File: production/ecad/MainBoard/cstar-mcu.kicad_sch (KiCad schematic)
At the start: 61 parts, among them J1 USB_C_Receptacle_USB2.0, J25 TYPE-C-31-M-12, J3 RX connect, J31 TYPE-C-31-M-12, J4 TX connect, J5 Ultra_1, J6 Ultra_2, J7 Ultra_3, J8 Ultra_4, Q1 AO3400A, Q2 AO3400A, Q3 AO3400A, Q4 AO3400A, SW1 SW_Push, SW2 SW_Push, SW3 SW_Push, SW4 SW_Push, U1 ESP32-WROOM-32UE_M113EH6400UH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, U2 CP2102N-A01-GQFN28, U3 TXB0104DR, U4 CP2102N-A01-GQFN28, U5 TXB0104DR, U6 ESP32-WROOM-32UE_M113EH6400UH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

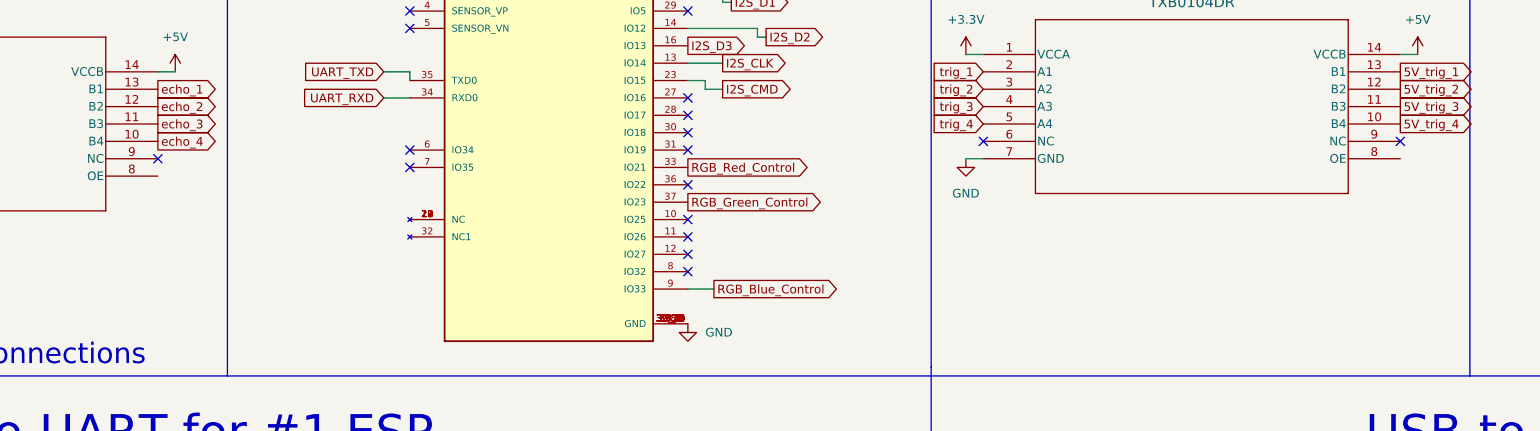
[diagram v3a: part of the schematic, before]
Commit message: OE to ground
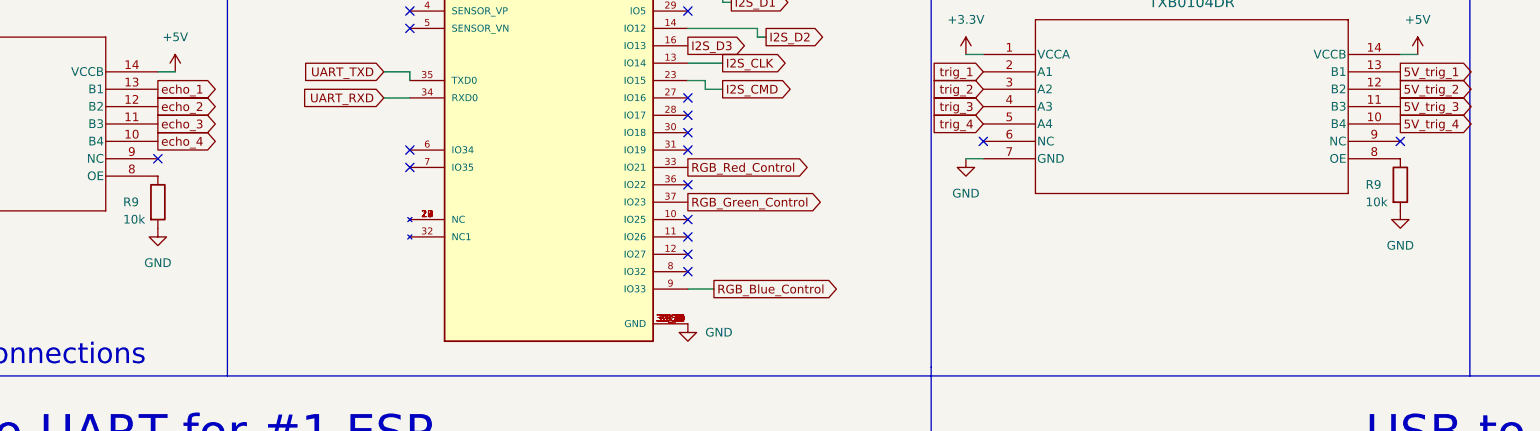
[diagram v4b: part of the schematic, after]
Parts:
- added R9 (x2): 10k, Resistor_SMD:R_0805_2012Metric, symbol Device:R
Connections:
- net GND: now also R9.2, R9.2
- net at U5.8 (OE): now also R9.1
- net at U3.8 (OE): now also R9.1
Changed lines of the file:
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@@
+    )
+  )
+  (symbol (lib_id "Device:R") (at 96.52 71.12 0) (unit 1)
+    (in_bom yes) (on_board yes) (dnp no)
+    (property "Reference" "R9" (at 91.44 71.12 0)
+      (effects (font (size 1.27 1.27)) (justify left))
+    )
+    (property "Value" "10k" (at 91.44 73.66 0)
+      (effects (font (size 1.27 1.27)) (justify left))
+    )
+    (property "Footprint" "Resistor_SMD:R_0805_2012Metric" (at 94.742 71.12 90)
+      (effects (font (size 1.27 1.27)) hide)
+    )
+    (property "Datasheet" "~" (at 96.52 71.12 0)
+      (effects (font (size 1.27 1.27)) hide)
+    )
+    (pin "1")
+    (pin "2")
+    (instances
+      (project "cstar-mcu"
+        (path "/889d461f-2713-421f-88e2-0d0ce2e66089"
+          (reference "R9") (unit 1)
+        )
+      )
+      (project "CSTAR"
+        (path "/cd9fa943-c6eb-468b-990c-ea873c442553/ab376fb8-b3cc-4961-835f-6ea621157706"
+          (reference "R45") (unit 1)
+        )
+      )
     )
   )
@@
         (path "/cd9fa943-c6eb-468b-990c-ea873c442553/ab376fb8-b3cc-4961-835f-6ea621157706"
           (reference "R49") (unit 1)
+        )
+      )
+    )
+  )
+  (symbol (lib_id "power:GND") (at 96.52 74.93 0) (unit 1)
+    (in_bom yes) (on_board yes) (dnp no) (fields_autoplaced)
+    (property "Reference" "#PWR038" (at 96.52 81.28 0)
+      (effects (font (size 1.27 1.27)) hide)
+    )
+    (property "Value" "GND" (at 96.52 80.01 0)
+      (effects (font (size 1.27 1.27)))
+    )
+    (property "Footprint" "" (at 96.52 74.93 0)
+      (effects (font (size 1.27 1.27)) hide)
+    )
+    (property "Datasheet" "" (at 96.52 74.93 0)
+      (effects (font (size 1.27 1.27)) hide)
+    )
+    (pin "1")
+    (instances
+      (project "cstar-mcu"
+        (path "/889d461f-2713-421f-88e2-0d0ce2e66089"
+          (reference "#PWR038") (unit 1)
+        )
+      )
+      (project "CSTAR"
+        (path "/cd9fa943-c6eb-468b-990c-ea873c442553/ab376fb8-b3cc-4961-835f-6ea621157706"
+          (reference "#PWR0110") (unit 1)
         )
       )
@@
     )
   )
+  (symbol (lib_id "Device:R") (at 278.13 68.58 0) (unit 1)
+    (in_bom yes) (on_board yes) (dnp no)
+    (property "Reference" "R9" (at 273.05 68.58 0)
+      (effects (font (size 1.27 1.27)) (justify left))
+    )
+    (property "Value" "10k" (at 273.05 71.12 0)
+      (effects (font (size 1.27 1.27)) (justify left))
+    )
+    (property "Footprint" "Resistor_SMD:R_0805_2012Metric" (at 276.352 68.58 90)
+      (effects (font (size 1.27 1.27)) hide)
+    )
+    (property "Datasheet" "~" (at 278.13 68.58 0)
+      (effects (font (size 1.27 1.27)) hide)
+    )
+    (pin "1")
+    (pin "2")
+    (instances
+      (project "cstar-mcu"
+        (path "/889d461f-2713-421f-88e2-0d0ce2e66089"
+          (reference "R9") (unit 1)
+        )
+      )
+      (project "CSTAR"
+        (path "/cd9fa943-c6eb-468b-990c-ea873c442553/ab376fb8-b3cc-4961-835f-6ea621157706"
+          (reference "R43") (unit 1)
+        )
+      )
+    )
+  )
   (symbol (lib_id "power:+5V") (at 24.13 15.24 90) (unit 1)
     (in_bom yes) (on_board yes) (dnp no) (fields_autoplaced)
@@
         )
       )
+    )
+  )
+  (symbol (lib_id "power:GND") (at 278.13 72.39 0) (unit 1)
+    (in_bom yes) (on_board yes) (dnp no) (fields_autoplaced)
+    (property "Reference" "#PWR038" (at 278.13 78.74 0)
+      (effects (font (size 1.27 1.27)) hide)
+    )
+    (property "Value" "GND" (at 278.13 77.47 0)
+      (effects (font (size 1.27 1.27)))
+    )
+    (property "Footprint" "" (at 278.13 72.39 0)
+      (effects (font (size 1.27 1.27)) hide)
+    )
+    (property "Datasheet" "" (at 278.13 72.39 0)
+      (effects (font (size 1.27 1.27)) hide)
+    )
+    (pin "1")
+    (instances
+      (project "cstar-mcu"
+        (path "/889d461f-2713-421f-88e2-0d0ce2e66089"
+          (reference "#PWR038") (unit 1)
+        )
+      )
+      (project "CSTAR"
+        (path "/cd9fa943-c6eb-468b-990c-ea873c442553/ab376fb8-b3cc-4961-835f-6ea621157706"
+          (reference "#PWR0113") (unit 1)
+        )
+      )

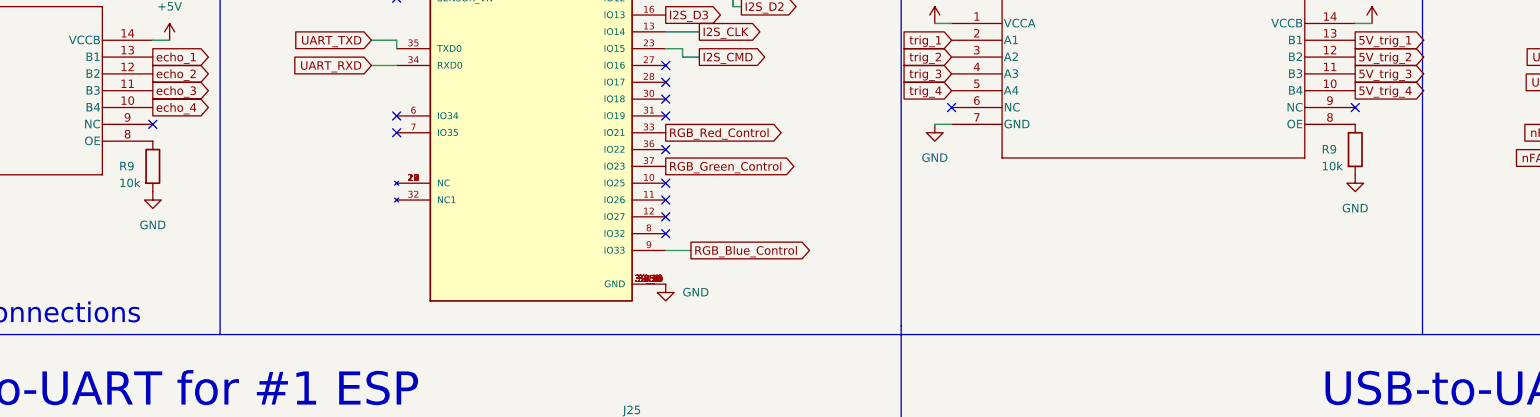
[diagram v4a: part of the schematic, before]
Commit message: fixed OE
talked to sean about the IC level shifter and fixed the open enable pin
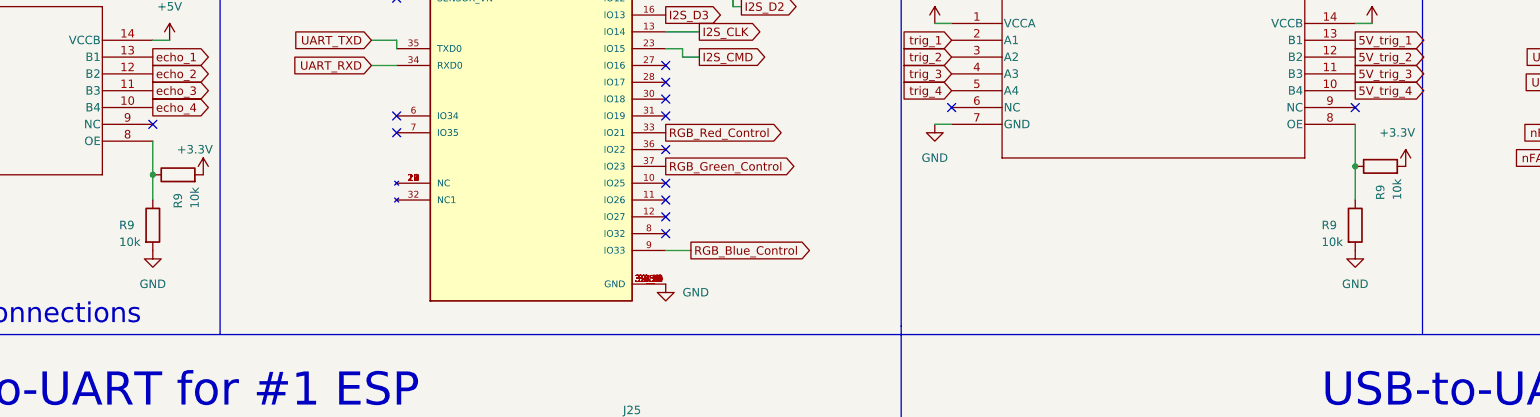
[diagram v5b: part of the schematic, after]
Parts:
- added R9 (x2): 10k, Resistor_SMD:R_0805_2012Metric, symbol Device:R
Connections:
- net +3.3V: now also R9.2, R9.2
- net at R9.1, U5.8 (OE): now also R9.1
- net at R9.1, U3.8 (OE): now also R9.1
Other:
- moved on the sheet: R9
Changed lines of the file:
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@@
   (junction (at 322.58 224.79) (diameter 0) (color 0 0 0 0)
   )
+  (junction (at 96.52 72.39) (diameter 0) (color 0 0 0 0)
+  )
   (junction (at 36.83 148.59) (diameter 0) (color 0 0 0 0)
   )
@@
   (junction (at 106.68 267.97) (diameter 0) (color 0 0 0 0)
   )
+  (junction (at 278.13 71.12) (diameter 0) (color 0 0 0 0)
+  )
   (junction (at 31.75 265.43) (diameter 0) (color 0 0 0 0)
   )
@@
     (stroke (width 0) (type default))
   )
+  (wire (pts (xy 278.13 71.12) (xy 278.13 64.77))
+    (stroke (width 0) (type default))
+  )
   (wire (pts (xy 361.95 33.02) (xy 370.84 33.02))
     (stroke (width 0) (type default))
@@
     (stroke (width 0) (type default))
   )
+  (wire (pts (xy 278.13 76.2) (xy 278.13 71.12))
+    (stroke (width 0) (type default))
+  )
   (wire (pts (xy 45.72 162.56) (xy 45.72 165.1))
     (stroke (width 0) (type default))
@@
     (stroke (width 0) (type default))
   )
+  (wire (pts (xy 96.52 72.39) (xy 96.52 67.31))
+    (stroke (width 0) (type default))
+  )
   (wire (pts (xy 173.99 148.59) (xy 181.61 148.59))
     (stroke (width 0) (type default))
@@
     (stroke (width 0) (type default))
   )
+  (wire (pts (xy 96.52 76.2) (xy 96.52 72.39))
+    (stroke (width 0) (type default))
+  )
   (wire (pts (xy 173.99 166.37) (xy 179.07 166.37))
     (stroke (width 0) (type default))
@@
     )
   )
+  (symbol (lib_id "Device:R") (at 100.33 72.39 90) (unit 1)
+    (in_bom yes) (on_board yes) (dnp no)
+    (property "Reference" "R9" (at 100.33 77.47 0)
+      (effects (font (size 1.27 1.27)) (justify left))
+    )
+    (property "Value" "10k" (at 102.87 77.47 0)
+      (effects (font (size 1.27 1.27)) (justify left))
+    )
+    (property "Footprint" "Resistor_SMD:R_0805_2012Metric" (at 100.33 74.168 90)
+      (effects (font (size 1.27 1.27)) hide)
+    )
+    (property "Datasheet" "~" (at 100.33 72.39 0)
+      (effects (font (size 1.27 1.27)) hide)
+    )
+    (pin "1")
+    (pin "2")
+    (instances
+      (project "cstar-mcu"
+        (path "/889d461f-2713-421f-88e2-0d0ce2e66089"
+          (reference "R9") (unit 1)
+        )
+      )
+      (project "CSTAR"
+        (path "/cd9fa943-c6eb-468b-990c-ea873c442553/ab376fb8-b3cc-4961-835f-6ea621157706"
+          (reference "R52") (unit 1)
+        )
+      )
+    )
+  )
   (symbol (lib_id "ESP32-WROOM-32UE_M113EH6400UH3Q0_:ESP32-WROOM-32UE_M113EH6400UH3Q0_") (at 341.63 63.5 0) (unit 1)
     (in_bom yes) (on_board yes) (dnp no) (fields_autoplaced)
@@
     )
   )
-  (symbol (lib_id "Device:R") (at 96.52 71.12 0) (unit 1)
+  (symbol (lib_id "Device:R") (at 96.52 80.01 0) (unit 1)
     (in_bom yes) (on_board yes) (dnp no)
-    (property "Reference" "R9" (at 91.44 71.12 0)
+    (property "Reference" "R9" (at 91.44 80.01 0)
       (effects (font (size 1.27 1.27)) (justify left))
     )
-    (property "Value" "10k" (at 91.44 73.66 0)
+    (property "Value" "10k" (at 91.44 82.55 0)
       (effects (font (size 1.27 1.27)) (justify left))
     )
-    (property "Footprint" "Resistor_SMD:R_0805_2012Metric" (at 94.742 71.12 90)
+    (property "Footprint" "Resistor_SMD:R_0805_2012Metric" (at 94.742 80.01 90)
       (effects (font (size 1.27 1.27)) hide)
     )
-    (property "Datasheet" "~" (at 96.52 71.12 0)
+    (property "Datasheet" "~" (at 96.52 80.01 0)
       (effects (font (size 1.27 1.27)) hide)
     )
@@
     )
   )
-  (symbol (lib_id "power:GND") (at 96.52 74.93 0) (unit 1)
+  (symbol (lib_id "power:GND") (at 96.52 83.82 0) (unit 1)
     (in_bom yes) (on_board yes) (dnp no) (fields_autoplaced)
-    (property "Reference" "#PWR038" (at 96.52 81.28 0)
+    (property "Reference" "#PWR038" (at 96.52 90.17 0)
       (effects (font (size 1.27 1.27)) hide)
     )
-    (property "Value" "GND" (at 96.52 80.01 0)
+    (property "Value" "GND" (at 96.52 88.9 0)
       (effects (font (size 1.27 1.27)))
     )
-    (property "Footprint" "" (at 96.52 74.93 0)
+    (property "Footprint" "" (at 96.52 83.82 0)
       (effects (font (size 1.27 1.27)) hide)
     )
-    (property "Datasheet" "" (at 96.52 74.93 0)
+    (property "Datasheet" "" (at 96.52 83.82 0)
       (effects (font (size 1.27 1.27)) hide)
     )
@@
     )
   )
+  (symbol (lib_id "power:+3.3V") (at 104.14 72.39 0) (unit 1)
+    (in_bom yes) (on_board yes) (dnp no)
+    (property "Reference" "#PWR0116" (at 104.14 76.2 0)
+      (effects (font (size 1.27 1.27)) hide)
+    )
+    (property "Value" "+3.3V" (at 102.87 68.58 0)
+      (effects (font (size 1.27 1.27)))
+    )
+    (property "Footprint" "" (at 104.14 72.39 0)
+      (effects (font (size 1.27 1.27)) hide)
+    )
+    (property "Datasheet" "" (at 104.14 72.39 0)
+      (effects (font (size 1.27 1.27)) hide)
+    )
+    (pin "1")
+    (instances
+      (project "CSTAR"
+        (path "/cd9fa943-c6eb-468b-990c-ea873c442553/ab376fb8-b3cc-4961-835f-6ea621157706"
+          (reference "#PWR0116") (unit 1)
+        )
+      )
+    )
+  )
   (symbol (lib_id "power:GND") (at 392.43 240.03 0) (unit 1)
     (in_bom yes) (on_board yes) (dnp no) (fields_autoplaced)
@@
     )
   )
-  (symbol (lib_id "Device:R") (at 278.13 68.58 0) (unit 1)
+  (symbol (lib_id "Device:R") (at 278.13 80.01 0) (unit 1)
     (in_bom yes) (on_board yes) (dnp no)
-    (property "Reference" "R9" (at 273.05 68.58 0)
+    (property "Reference" "R9" (at 273.05 80.01 0)
       (effects (font (size 1.27 1.27)) (justify left))
     )
-    (property "Value" "10k" (at 273.05 71.12 0)
+    (property "Value" "10k" (at 273.05 82.55 0)
       (effects (font (size 1.27 1.27)) (justify left))
     )
-    (property "Footprint" "Resistor_SMD:R_0805_2012Metric" (at 276.352 68.58 90)
+    (property "Footprint" "Resistor_SMD:R_0805_2012Metric" (at 276.352 80.01 90)
       (effects (font (size 1.27 1.27)) hide)
     )
-    (property "Datasheet" "~" (at 278.13 68.58 0)
+    (property "Datasheet" "~" (at 278.13 80.01 0)
       (effects (font (size 1.27 1.27)) hide)
     )
@@
     )
   )
+  (symbol (lib_id "power:+3.3V") (at 285.75 71.12 0) (unit 1)
+    (in_bom yes) (on_board yes) (dnp no)
+    (property "Reference" "#PWR0136" (at 285.75 74.93 0)
+      (effects (font (size 1.27 1.27)) hide)
+    )
+    (property "Value" "+3.3V" (at 284.48 66.04 0)
+      (effects (font (size 1.27 1.27)))
+    )
+    (property "Footprint" "" (at 285.75 71.12 0)
+      (effects (font (size 1.27 1.27)) hide)
+    )
+    (property "Datasheet" "" (at 285.75 71.12 0)
+      (effects (font (size 1.27 1.27)) hide)
+    )
+    (pin "1")
+    (instances
+      (project "CSTAR"
+        (path "/cd9fa943-c6eb-468b-990c-ea873c442553/ab376fb8-b3cc-4961-835f-6ea621157706"
+          (reference "#PWR0136") (unit 1)
+        )
+      )
+    )
+  )
   (symbol (lib_id "Device:R") (at 29.21 177.8 180) (unit 1)
     (in_bom yes) (on_board yes) (dnp no)
@@
     )
   )
+  (symbol (lib_id "Device:R") (at 281.94 71.12 90) (unit 1)
+    (in_bom yes) (on_board yes) (dnp no)
+    (property "Reference" "R9" (at 281.94 76.2 0)
+      (effects (font (size 1.27 1.27)) (justify left))
+    )
+    (property "Value" "10k" (at 284.48 76.2 0)
+      (effects (font (size 1.27 1.27)) (justify left))
+    )
+    (property "Footprint" "Resistor_SMD:R_0805_2012Metric" (at 281.94 72.898 90)
+      (effects (font (size 1.27 1.27)) hide)
+    )
+    (property "Datasheet" "~" (at 281.94 71.12 0)
+      (effects (font (size 1.27 1.27)) hide)
+    )
+    (pin "1")
+    (pin "2")
+    (instances
+      (project "cstar-mcu"
+        (path "/889d461f-2713-421f-88e2-0d0ce2e66089"
+          (reference "R9") (unit 1)
+        )
+      )
+      (project "CSTAR"
+        (path "/cd9fa943-c6eb-468b-990c-ea873c442553/ab376fb8-b3cc-4961-835f-6ea621157706"
+          (reference "R53") (unit 1)
+        )
+      )
+    )
+  )
   (symbol (lib_id "Device:R") (at 195.58 133.35 0) (unit 1)
     (in_bom yes) (on_board yes) (dnp no)
@@
     )
   )
-  (symbol (lib_id "power:GND") (at 278.13 72.39 0) (unit 1)
+  (symbol (lib_id "power:GND") (at 278.13 83.82 0) (unit 1)
     (in_bom yes) (on_board yes) (dnp no) (fields_autoplaced)
-    (property "Reference" "#PWR038" (at 278.13 78.74 0)
+    (property "Reference" "#PWR038" (at 278.13 90.17 0)
       (effects (font (size 1.27 1.27)) hide)
     )
-    (property "Value" "GND" (at 278.13 77.47 0)
+    (property "Value" "GND" (at 278.13 88.9 0)
       (effects (font (size 1.27 1.27)))
     )
-    (property "Footprint" "" (at 278.13 72.39 0)
+    (property "Footprint" "" (at 278.13 83.82 0)
       (effects (font (size 1.27 1.27)) hide)
     )
-    (property "Datasheet" "" (at 278.13 72.39 0)
+    (property "Datasheet" "" (at 278.13 83.82 0)
       (effects (font (size 1.27 1.27)) hide)
     )

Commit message: layout adjustments
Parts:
- removed J1: USB_C_Receptacle_USB2.0, CSTAR-MainBoard-Footprints:USBCONN-GCT_USB4105GFA, symbol Connector:USB_C_Receptacle_USB2.0
- removed R8, R9: 5.1k, Resistor_SMD:R_0805_2012Metric, symbol Device:R
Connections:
- no-connect marks 59 -> 56
